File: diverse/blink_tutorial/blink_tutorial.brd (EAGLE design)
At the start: 39.6 x 29.9 mm, 12 parts, among them T1 BC547, T2 BC547

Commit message: reworked structure
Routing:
- added copper zone on layer 1, net GND
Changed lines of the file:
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@@
 <contactref element="T1" pad="1"/>
 <contactref element="JP1" pad="2"/>
-<wire x1="21.844" y1="9.652" x2="20.828" y2="26.924" width="0" layer="19" extent="1-1"/>
-<wire x1="12.7" y1="4.318" x2="21.844" y2="9.652" width="0" layer="19" extent="1-1"/>
+<polygon width="0.254" layer="1">
+<vertex x="0" y="29.972"/>
+<vertex x="39.624" y="29.972"/>
+<vertex x="39.624" y="0"/>
+<vertex x="0" y="0"/>
+</polygon>
 </signal>
 </signals>

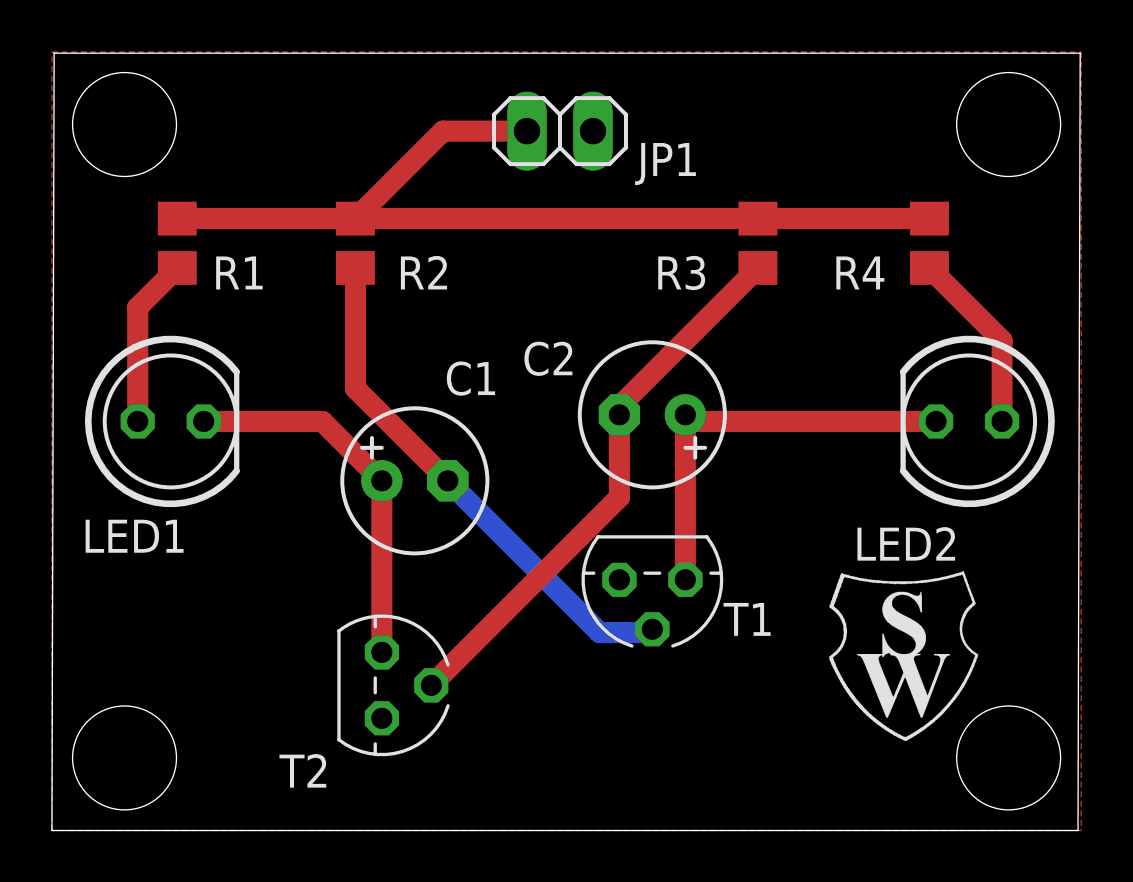
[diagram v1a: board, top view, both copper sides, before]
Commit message: updated wemos and diverse boards
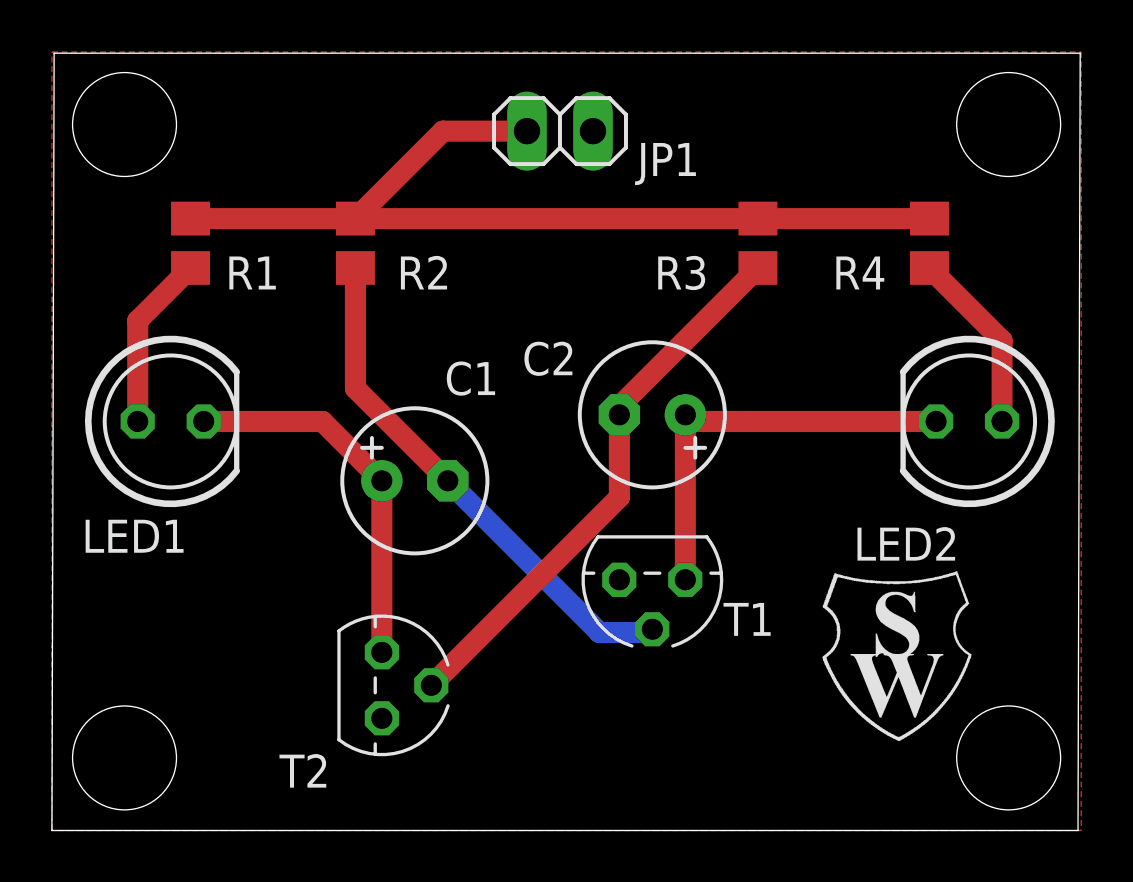
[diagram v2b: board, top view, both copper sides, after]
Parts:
- U$1: value (none) -> SIG1
- moved R1 0.51 mm to (5.33, 22.6)
- moved U$1 0.25 mm to (29.5, 3.30)
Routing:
- net N$1: track 37.0 -> 36.4 mm
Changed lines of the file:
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@@
 <?xml version="1.0" encoding="utf-8"?>
 <!DOCTYPE eagle SYSTEM "eagle.dtd">
-<eagle version="9.3.0">
+<eagle version="9.6.2">
 <drawing>
 <settings>
@@
 <setting verticaltext="up"/>
 </settings>
-<grid distance="10" unitdist="mil" unit="mil" style="lines" multiple="1" display="yes" altdistance="5" altunitdist="mil" altunit="mil"/>
+<grid distance="10" unitdist="mil" unit="mm" style="lines" multiple="1" display="yes" altdistance="5" altunitdist="mil" altunit="mil"/>
 <layers>
 <layer number="1" name="Top" color="4" fill="1" visible="yes" active="yes"/>
@@
 </class>
 </classes>
-<designrules name="default">
+<designrules name="default *">
 <description language="de">&lt;b&gt;EAGLE Design Rules&lt;/b&gt;
 &lt;p&gt;
@@
 <param name="mtCopper" value="0.035mm 0.035mm 0.035mm 0.035mm 0.035mm 0.035mm 0.035mm 0.035mm 0.035mm 0.035mm 0.035mm 0.035mm 0.035mm 0.035mm 0.035mm 0.035mm"/>
 <param name="mtIsolate" value="1.5mm 0.15mm 0.2mm 0.15mm 0.2mm 0.15mm 0.2mm 0.15mm 0.2mm 0.15mm 0.2mm 0.15mm 0.2mm 0.15mm 0.2mm"/>
-<param name="mdWireWire" value="6mil"/>
+<param name="mdWireWire" value="0.5mm"/>
 <param name="mdWirePad" value="6mil"/>
 <param name="mdWireVia" value="6mil"/>
@@
 <attribute name="VALUE" x="32.1056" y="17.5514" size="1.27" layer="27" ratio="10" rot="R180"/>
 </element>
-<element name="R1" library="rcl" library_urn="urn:adsk.eagle:library:334" package="R0805" package3d_urn="urn:adsk.eagle:package:23553/2" value="680" x="4.826" y="22.606" smashed="yes" rot="R90">
-<attribute name="NAME" x="8.255" y="22.098" size="1.27" layer="25" font="vector" ratio="12" rot="R180"/>
-<attribute name="SPICEPREFIX" value="R" x="23.876" y="39.116" size="1.778" layer="27" rot="R90" display="off"/>
-<attribute name="VALUE" x="7.366" y="21.971" size="1.27" layer="27" rot="R90"/>
+<element name="R1" library="rcl" library_urn="urn:adsk.eagle:library:334" package="R0805" package3d_urn="urn:adsk.eagle:package:23553/2" value="680" x="5.334" y="22.606" smashed="yes" rot="R90">
+<attribute name="NAME" x="8.763" y="22.098" size="1.27" layer="25" font="vector" ratio="12" rot="R180"/>
+<attribute name="SPICEPREFIX" value="R" x="24.384" y="39.116" size="1.778" layer="27" rot="R90" display="off"/>
+<attribute name="VALUE" x="7.874" y="21.971" size="1.27" layer="27" rot="R90"/>
 </element>
 <element name="R2" library="rcl" library_urn="urn:adsk.eagle:library:334" package="R0805" package3d_urn="urn:adsk.eagle:package:23553/2" value="2k7" x="11.684" y="22.606" smashed="yes" rot="R90">
@@
 <attribute name="VALUE" x="11.43" y="2.413" size="1.27" layer="27" ratio="10" rot="R270"/>
 </element>
-<element name="U$1" library="SWI_COMMONS" package="BRAND_SWI_5X7" value="" x="29.718" y="3.302" smashed="yes"/>
+<element name="U$1" library="SWI_COMMONS" package="BRAND_SWI_5X7" value="SIG1" x="29.464" y="3.302" smashed="yes"/>
 </elements>
 <signals>
@@
 <wire x1="18.288" y1="26.924" x2="15.052" y2="26.924" width="0.8128" layer="1"/>
 <wire x1="15.052" y1="26.924" x2="11.684" y2="23.556" width="0.8128" layer="1"/>
-<wire x1="11.684" y1="23.556" x2="4.826" y2="23.556" width="0.8128" layer="1"/>
+<wire x1="11.684" y1="23.556" x2="5.334" y2="23.556" width="0.8128" layer="1"/>
 <wire x1="11.684" y1="23.556" x2="27.178" y2="23.556" width="0.8128" layer="1"/>
 <wire x1="27.178" y1="23.556" x2="33.782" y2="23.556" width="0.8128" layer="1"/>
@@
 <contactref element="R1" pad="1"/>
 <contactref element="LED1" pad="A"/>
-<wire x1="4.826" y1="21.656" x2="3.302" y2="20.132" width="0.8128" layer="1"/>
-<wire x1="3.302" y1="20.132" x2="3.302" y2="15.748" width="0.8128" layer="1"/>
+<wire x1="5.334" y1="21.656" x2="3.302" y2="19.624" width="0.8128" layer="1"/>
+<wire x1="3.302" y1="19.624" x2="3.302" y2="15.748" width="0.8128" layer="1"/>
 </signal>
 <signal name="N$3">

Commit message: final blink tutorial board
changed to bottom layer connections
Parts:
- moved T1 1.80 mm to (24.4, 8.38), turned to 270 degrees
- moved JP1 1.02 mm to (19.6, 25.9)
- moved R1 0.76 mm to (6.10, 22.6), flipped to the bottom
- moved R4 0.51 mm to (33.3, 22.6), flipped to the bottom
- flipped R2 to the bottom
- flipped R3 to the bottom
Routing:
- net GND: track 0.00 -> 35.0 mm, vias 0 -> 5
- net N$1: track 36.4 -> 30.3 mm
- net N$7: track 20.0 -> 22.8 mm
- net N$6: track 21.3 -> 22.3 mm
- added copper zone on layer 16, net GND
- removed copper zone on layer 1, net GND

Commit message: modified for cnc manufacturing
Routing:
- net GND: track 35.0 -> 22.0 mm, vias 5 -> 6
- net N$7: track 22.8 -> 35.6 mm
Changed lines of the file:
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@@
 <contactref element="R2" pad="2"/>
 <contactref element="R1" pad="2"/>
-<wire x1="18.288" y1="25.908" x2="17.018" y2="24.638" width="0.8128" layer="16"/>
-<wire x1="16.51" y1="25.146" x2="14.92" y2="23.556" width="0.8128" layer="16"/>
-<wire x1="14.92" y1="23.556" x2="11.684" y2="23.556" width="0.8128" layer="16"/>
-<wire x1="11.684" y1="23.556" x2="6.096" y2="23.556" width="0.8128" layer="16"/>
-<wire x1="27.178" y1="23.556" x2="18.1" y2="23.556" width="0.8128" layer="16"/>
-<wire x1="18.1" y1="23.556" x2="17.018" y2="24.638" width="0.8128" layer="16"/>
-<wire x1="17.018" y1="24.638" x2="16.51" y2="25.146" width="0.8128" layer="16"/>
-<wire x1="27.178" y1="23.556" x2="33.274" y2="23.556" width="0.8128" layer="16"/>
+<wire x1="18.288" y1="25.908" x2="17.018" y2="24.638" width="1.27" layer="16"/>
+<wire x1="16.51" y1="25.146" x2="14.92" y2="23.556" width="1.27" layer="16"/>
+<wire x1="14.92" y1="23.556" x2="11.684" y2="23.556" width="1.27" layer="16"/>
+<wire x1="11.684" y1="23.556" x2="6.096" y2="23.556" width="1.27" layer="16"/>
+<wire x1="27.178" y1="23.556" x2="18.1" y2="23.556" width="1.27" layer="16"/>
+<wire x1="18.1" y1="23.556" x2="17.018" y2="24.638" width="1.27" layer="16"/>
+<wire x1="17.018" y1="24.638" x2="16.51" y2="25.146" width="1.27" layer="16"/>
+<wire x1="27.178" y1="23.556" x2="33.274" y2="23.556" width="1.27" layer="16"/>
 </signal>
 <signal name="N$2">
 <contactref element="R1" pad="1"/>
 <contactref element="LED1" pad="A"/>
-<wire x1="6.096" y1="21.656" x2="3.302" y2="18.862" width="0.8128" layer="16"/>
-<wire x1="3.302" y1="18.862" x2="3.302" y2="15.748" width="0.8128" layer="16"/>
+<wire x1="6.096" y1="21.656" x2="3.302" y2="18.862" width="1.27" layer="16"/>
+<wire x1="3.302" y1="18.862" x2="3.302" y2="15.748" width="1.27" layer="16"/>
 </signal>
 <signal name="N$3">
 <contactref element="R4" pad="1"/>
 <contactref element="LED2" pad="A"/>
-<wire x1="33.274" y1="21.656" x2="36.576" y2="18.354" width="0.8128" layer="16"/>
-<wire x1="36.576" y1="18.354" x2="36.576" y2="15.748" width="0.8128" layer="16"/>
+<wire x1="33.274" y1="21.656" x2="36.576" y2="18.354" width="1.27" layer="16"/>
+<wire x1="36.576" y1="18.354" x2="36.576" y2="15.748" width="1.27" layer="16"/>
 </signal>
 <signal name="N$4">
@@
 <contactref element="T2" pad="3"/>
 <contactref element="C1" pad="+"/>
-<wire x1="5.842" y1="15.748" x2="10.414" y2="15.748" width="0.8128" layer="16"/>
-<wire x1="10.414" y1="15.748" x2="12.7" y2="13.462" width="0.8128" layer="16"/>
-<wire x1="12.7" y1="13.462" x2="12.7" y2="6.858" width="0.8128" layer="16"/>
+<wire x1="5.842" y1="15.748" x2="10.414" y2="15.748" width="1.27" layer="16"/>
+<wire x1="10.414" y1="15.748" x2="12.7" y2="13.462" width="1.27" layer="16"/>
+<wire x1="12.7" y1="13.462" x2="12.7" y2="6.858" width="1.27" layer="16"/>
 </signal>
 <signal name="N$5">
@@
 <contactref element="T1" pad="3"/>
 <contactref element="C2" pad="+"/>
-<wire x1="24.384" y1="16.002" x2="33.782" y2="16.002" width="0.8128" layer="16"/>
+<wire x1="24.384" y1="16.002" x2="33.782" y2="16.002" width="1.27" layer="16"/>
 <wire x1="33.782" y1="16.002" x2="34.036" y2="15.748" width="0.8128" layer="16"/>
-<wire x1="24.384" y1="16.002" x2="24.384" y2="9.652" width="0.8128" layer="16"/>
+<wire x1="24.384" y1="16.002" x2="24.384" y2="9.652" width="1.27" layer="16"/>
 </signal>
 <signal name="N$6">
@@
 <contactref element="C2" pad="-"/>
 <contactref element="T2" pad="2"/>
-<wire x1="21.844" y1="16.002" x2="21.844" y2="18.034" width="0.8128" layer="16"/>
-<wire x1="25.466" y1="21.656" x2="27.178" y2="21.656" width="0.8128" layer="16"/>
-<wire x1="21.844" y1="18.034" x2="25.466" y2="21.656" width="0.8128" layer="16"/>
+<wire x1="21.844" y1="16.002" x2="21.844" y2="18.034" width="1.27" layer="16"/>
+<wire x1="25.466" y1="21.656" x2="27.178" y2="21.656" width="1.27" layer="16"/>
+<wire x1="21.844" y1="18.034" x2="25.466" y2="21.656" width="1.27" layer="16"/>
 <wire x1="21.844" y1="16.002" x2="21.844" y2="12.827" width="0.8128" layer="1"/>
 <wire x1="21.844" y1="12.827" x2="14.605" y2="5.588" width="0.8128" layer="1"/>
@@
 <contactref element="C1" pad="-"/>
 <contactref element="T1" pad="2"/>
-<wire x1="11.684" y1="21.656" x2="15.24" y2="18.1" width="0.8128" layer="16"/>
-<wire x1="15.24" y1="18.1" x2="15.24" y2="13.462" width="0.8128" layer="16"/>
-<wire x1="15.24" y1="13.462" x2="20.32" y2="8.382" width="0.8128" layer="16"/>
-<wire x1="20.32" y1="8.382" x2="26.289" y2="8.382" width="0.8128" layer="16"/>
+<wire x1="11.684" y1="21.656" x2="15.24" y2="18.1" width="1.27" layer="16"/>
+<wire x1="15.24" y1="18.1" x2="15.24" y2="13.462" width="1.27" layer="16"/>
+<wire x1="26.289" y1="8.382" x2="27.94" y2="6.731" width="1.27" layer="16"/>
+<wire x1="27.94" y1="6.731" x2="27.94" y2="3.81" width="1.27" layer="16"/>
+<wire x1="27.94" y1="3.81" x2="26.67" y2="2.54" width="1.27" layer="16"/>
+<wire x1="26.67" y1="2.54" x2="21.59" y2="2.54" width="1.27" layer="16"/>
+<wire x1="21.59" y1="2.54" x2="19.05" y2="5.08" width="1.27" layer="16"/>
+<wire x1="19.05" y1="5.08" x2="19.05" y2="10.16" width="1.27" layer="16"/>
+<wire x1="19.05" y1="10.16" x2="15.748" y2="13.462" width="1.27" layer="16"/>
+<wire x1="15.748" y1="13.462" x2="15.24" y2="13.462" width="1.27" layer="16"/>
 </signal>
 <signal name="GND">
@@
 <via x="12.7" y="17.78" extent="1-16" drill="0.8" diameter="1.778"/>
 <via x="13.97" y="26.67" extent="1-16" drill="0.8" diameter="1.778"/>
-<via x="21.59" y="21.59" extent="1-16" drill="0.8" diameter="1.778"/>
+<via x="17.78" y="20.32" extent="1-16" drill="0.8" diameter="1.778"/>
 <via x="30.48" y="17.78" extent="1-16" drill="0.8" diameter="1.778"/>
 <via x="29.21" y="13.97" extent="1-16" drill="0.8" diameter="1.778"/>
-<wire x1="12.7" y1="17.78" x2="16.51" y2="21.59" width="0.8128" layer="1"/>
-<wire x1="16.51" y1="21.59" x2="21.59" y2="21.59" width="0.8128" layer="1"/>
-<wire x1="21.59" y1="21.59" x2="19.05" y2="21.59" width="0.8128" layer="1"/>
-<wire x1="19.05" y1="21.59" x2="13.97" y2="26.67" width="0.8128" layer="1"/>
-<wire x1="21.59" y1="21.59" x2="22.86" y2="21.59" width="0.8128" layer="1"/>
-<wire x1="22.86" y1="21.59" x2="26.67" y2="17.78" width="0.8128" layer="1"/>
-<wire x1="26.67" y1="17.78" x2="30.48" y2="17.78" width="0.8128" layer="1"/>
 <wire x1="30.48" y1="17.78" x2="30.48" y2="15.24" width="0.8128" layer="1"/>
 <wire x1="30.48" y1="15.24" x2="29.21" y2="13.97" width="0.8128" layer="1"/>
+<via x="7.62" y="10.16" extent="1-16" drill="0.8" diameter="1.778"/>
+<wire x1="12.7" y1="17.78" x2="7.62" y2="12.7" width="0.8128" layer="1"/>
+<wire x1="7.62" y1="12.7" x2="7.62" y2="10.16" width="0.8128" layer="1"/>
+<wire x1="17.78" y1="20.32" x2="13.97" y2="24.13" width="0.8128" layer="1"/>
+<wire x1="13.97" y1="24.13" x2="13.97" y2="26.67" width="0.8128" layer="1"/>
+<wire x1="17.78" y1="20.32" x2="12.7" y2="17.78" width="0" layer="19" extent="1-1"/>
 </signal>
 </signals>

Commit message: modified layout for manufacturing
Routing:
- net N$6: track 22.3 -> 22.7 mm, vias 0 -> 2
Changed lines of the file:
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@@
 <wire x1="25.466" y1="21.656" x2="27.178" y2="21.656" width="1.27" layer="16"/>
 <wire x1="21.844" y1="18.034" x2="25.466" y2="21.656" width="1.27" layer="16"/>
-<wire x1="21.844" y1="16.002" x2="21.844" y2="12.827" width="0.8128" layer="1"/>
-<wire x1="21.844" y1="12.827" x2="14.605" y2="5.588" width="0.8128" layer="1"/>
+<via x="15.24" y="8.89" extent="1-16" drill="0.8" diameter="1.778"/>
+<via x="19.05" y="13.97" extent="1-16" drill="0.8" diameter="1.778"/>
+<wire x1="15.24" y1="8.89" x2="19.05" y2="12.7" width="1.27" layer="1"/>
+<wire x1="19.05" y1="12.7" x2="19.05" y2="13.97" width="1.27" layer="1"/>
+<wire x1="14.605" y1="5.588" x2="15.24" y2="6.223" width="1.27" layer="16"/>
+<wire x1="15.24" y1="8.89" x2="15.24" y2="6.223" width="1.27" layer="16"/>
+<wire x1="19.05" y1="13.97" x2="21.082" y2="16.002" width="1.27" layer="16"/>
+<wire x1="21.082" y1="16.002" x2="21.844" y2="16.002" width="1.27" layer="16"/>
 </signal>
 <signal name="N$7">

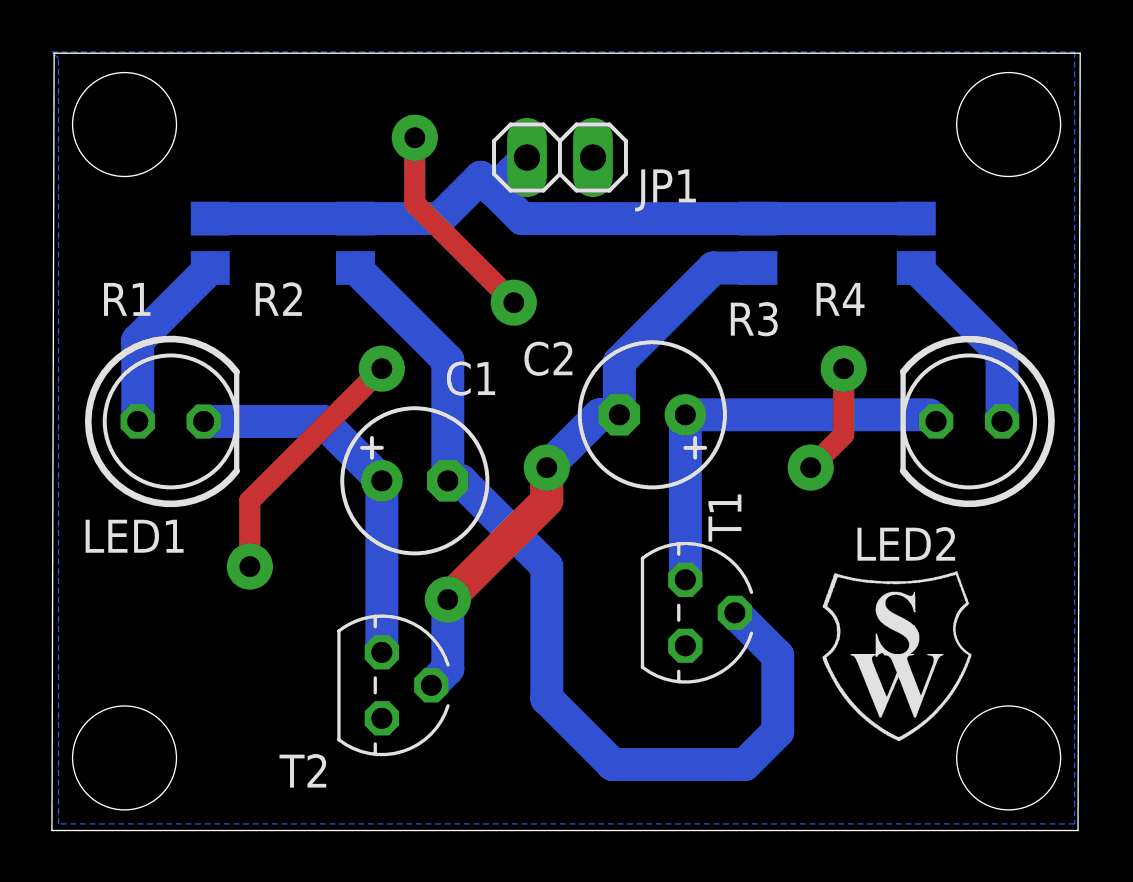
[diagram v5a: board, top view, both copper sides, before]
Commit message: changed resistor footprint to 1206
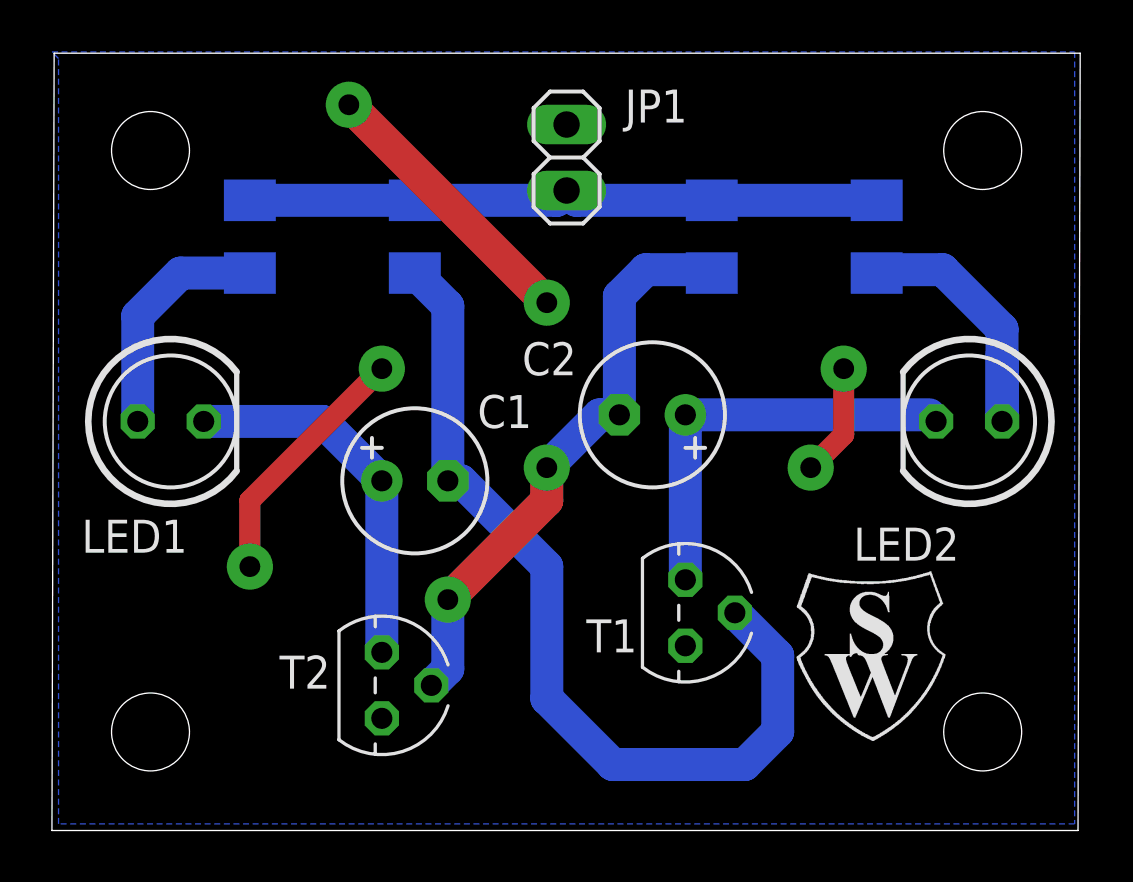
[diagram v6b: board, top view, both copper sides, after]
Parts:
- R1, R2, R3, R4: device rcl:R0805 -> SWI_COMMONS:M1206
- moved R2 2.30 mm to (14.0, 22.9)
- moved R3 1.80 mm to (25.4, 22.9)
- moved R4 1.55 mm to (31.8, 22.9)
- moved R1 1.55 mm to (7.62, 22.9)
- moved U$1 1.00 mm to (28.5, 3.30)
- moved JP1 0.25 mm to (19.8, 25.9), turned to 90 degrees
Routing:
- net N$1: track 30.3 -> 24.4 mm
- net N$3: track 7.28 -> 12.0 mm
- net GND: track 22.0 -> 24.8 mm
- net N$2: track 7.07 -> 9.06 mm
- net N$7: track 35.6 -> 34.5 mm
